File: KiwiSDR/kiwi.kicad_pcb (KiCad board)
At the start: 6 copper layers, 117 x 55 mm, 173 parts, among them J1 TB_2, J2 SMA, J3 SMA, J4 DNL U.FL, J5 DNL U.FL, J6 POWER JACK 2.1MM, T301 CMC 500uH 1A, U1 Artix-7 A35, U101 SE4150L, U104 LP5907 3.3V 250mA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

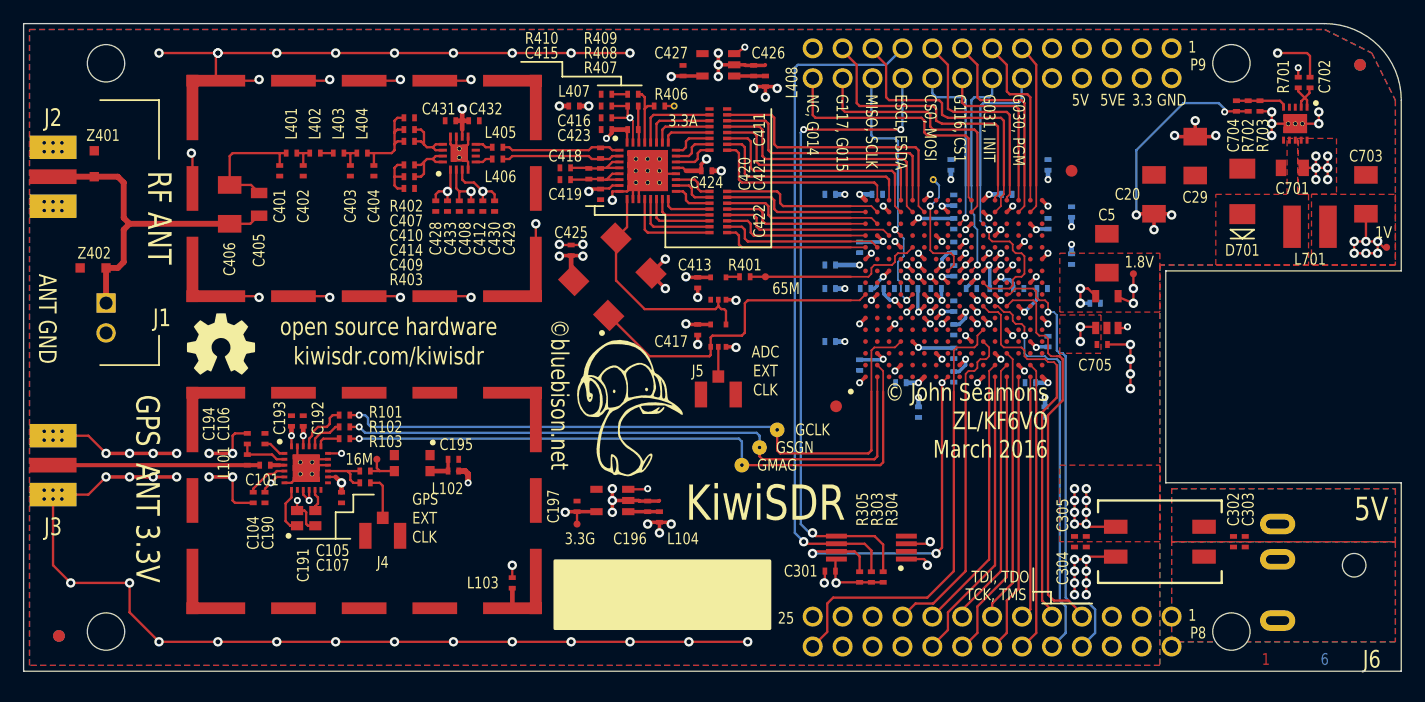
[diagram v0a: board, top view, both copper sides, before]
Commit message: long overdue update to v1.0 PCB files
These are the files used in the current production PCBs.
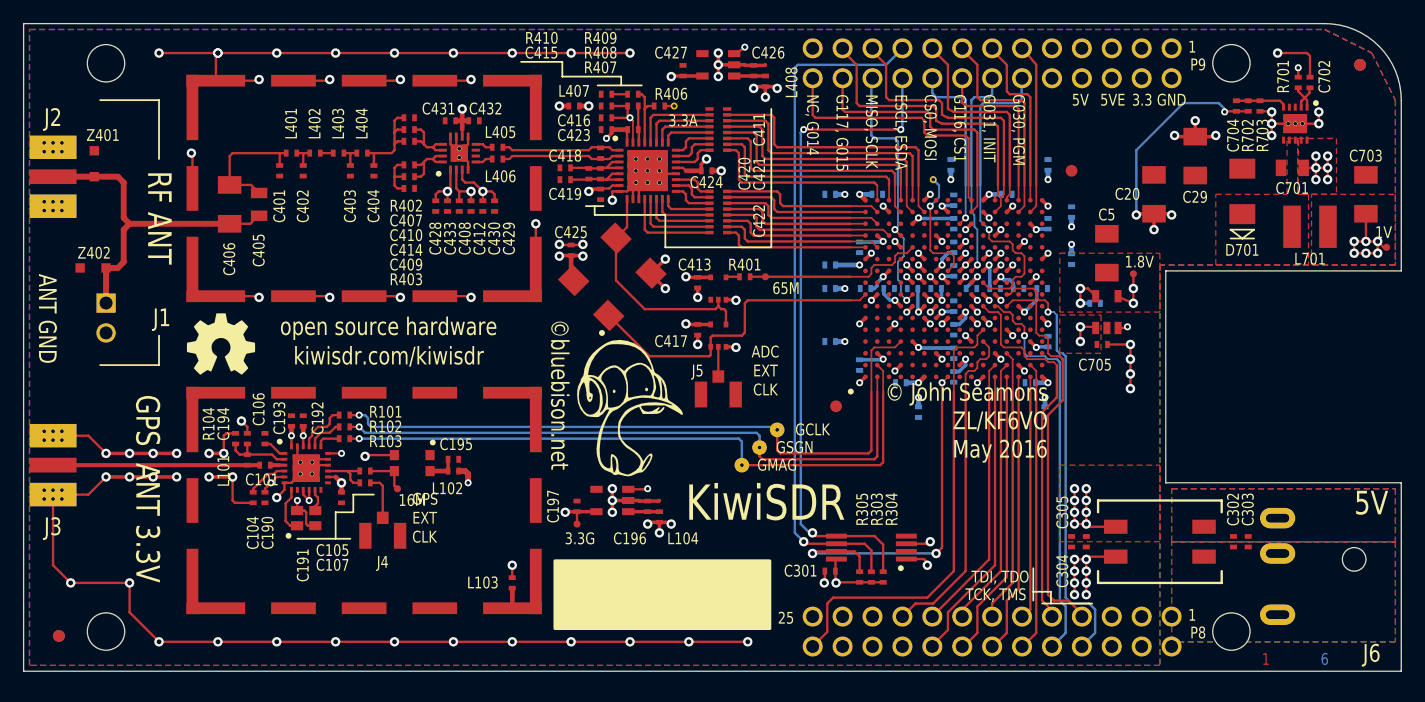
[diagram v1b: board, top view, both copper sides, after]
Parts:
- added R104: 1K5, kiwi-SM0402, F.Cu at (94.0, 107.8)
- moved TP101 3.05 mm to (107.8, 112.0)
- moved J6 0.50 mm to (193.0, 118.0)
- moved C303 0.25 mm to (180.0, 116.5)
- moved C304 0.25 mm to (165.0, 116.5)
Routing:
- net GND: track 296.6 -> 300.9 mm, vias 116 -> 119
- net /GPS/GBIAS: track 4.22 -> 5.91 mm
- net /GPS/TCXO2: track 3.14 -> 3.64 mm
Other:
- board text added: "KiwiSDR V1.0 2-May-2016"
- board text added: "© John Seamons ZL/KF6VO May 2016"
- board text removed: "KiwiSDR prototype v0.5 22-Feb-2016"
- board text removed: "PROTOTYPE ONLY NOT FOR QUANTITY PRODUCTION"
- board text removed: "© John Seamons ZL/KF6VO March 2016"
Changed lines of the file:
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@@
 (kicad_pcb (version 3) (host pcbnew "(2013-mar-25)-stable")
   (general
-    (links 555)
+    (links 557)
     (no_connects 0)
     (area 66.587499 53.8 205.779764 127.775)
     (thickness 1.6)
-    (drawings 73)
-    (tracks 1536)
+    (drawings 72)
+    (tracks 1547)
     (zones 0)
-    (modules 173)
+    (modules 174)
     (nets 120)
   )
@@
   )
   (module kiwi-TP_600 (layer Top)
-    (at 106 109.5)
+    (at 107.75 112)
     (solder_mask_margin 0.05)
     (clearance 0.05)
@@
     (clearance 0.05)
     (attr smd)
-    (fp_text reference C106 (at -1.25 3.5 270) (layer F.SilkS)
+    (fp_text reference C106 (at -2.5 0.5 270) (layer F.SilkS)
       (effects (font (size 1 0.8) (thickness 0.15)))
     )
@@
     (clearance 0.05)
     (attr smd)
-    (fp_text reference L101 (at -0.2 -2 90) (layer F.SilkS)
+    (fp_text reference L101 (at -0.95 -2 90) (layer F.SilkS)
       (effects (font (size 1 0.8) (thickness 0.15)))
     )
@@
     (clearance 0.05)
     (attr smd)
-    (fp_text reference C194 (at -1.25 3.25 270) (layer F.SilkS)
+    (fp_text reference C194 (at -1.25 2 270) (layer F.SilkS)
       (effects (font (size 1 0.8) (thickness 0.15)))
     )
@@
   )
   (module kiwi-SM0402 (layer Top)
-    (at 179.75 116.5 270)
+    (at 180 116.5 270)
     (solder_mask_margin 0.05)
     (clearance 0.05)
     (attr smd)
-    (fp_text reference C303 (at -2.75 -0.25 270) (layer F.SilkS)
+    (fp_text reference C303 (at -2.75 0 270) (layer F.SilkS)
       (effects (font (size 1 0.8) (thickness 0.15)))
     )
@@
   )
   (module kiwi-SM0402 (layer Top)
-    (at 165.25 116.5 270)
+    (at 165 116.5 270)
     (solder_mask_margin 0.05)
     (clearance 0.05)
     (attr smd)
-    (fp_text reference C304 (at 2.25 1 270) (layer F.SilkS)
+    (fp_text reference C304 (at 2.5 0.75 270) (layer F.SilkS)
       (effects (font (size 1 0.8) (thickness 0.15)))
     )
@@
     (clearance 0.05)
     (attr smd)
-    (fp_text reference C305 (at -2.25 2 270) (layer F.SilkS)
+    (fp_text reference C305 (at -2.5 2 270) (layer F.SilkS)
       (effects (font (size 1 0.8) (thickness 0.15)))
     )
@@
   )
   (module kiwi-JACK_2_1MM_TH (layer Top)
-    (at 193 118.5)
+    (at 193 118)
     (descr "Best JACK_2_1MM_TH footprint")
     (solder_mask_margin 0.05)
@@
     )
   )
+  (module kiwi-SM0402 (layer Top)
+    (at 94 107.75 90)
+    (solder_mask_margin 0.05)
+    (clearance 0.05)
+    (attr smd)
+    (fp_text reference R104 (at 1.25 -2.25 90) (layer F.SilkS)
+      (effects (font (size 1 0.8) (thickness 0.15)))
+    )
+    (fp_text value 1K5 (at 0 0 90) (layer F.SilkS) hide
+      (effects (font (size 1 0.8) (thickness 0.15)))
+    )
+    (pad 1 smd rect (at -0.45 0 90) (size 0.4 0.6)
+      (layers Top F.Paste F.Mask)
+      (net 62 /GPS/GBIAS)
+    )
+    (pad 2 smd rect (at 0.45 0 90) (size 0.4 0.6)
+      (layers Top F.Paste F.Mask)
+      (net 116 GND)
+    )
+  )
   (gr_line (start 163.25 120.75) (end 163.25 121.75) (angle 90) (layer F.SilkS) (width 0.15))
   (gr_line (start 161.75 120.75) (end 163.25 120.75) (angle 90) (layer F.SilkS) (width 0.15))
@@
     (effects (font (size 1 0.8) (thickness 0.15)))
   )
-  (gr_text 5V (at 189 113.75) (layer F.SilkS)
+  (gr_text 5V (at 189 113.25) (layer F.SilkS)
     (effects (font (size 2 1.6) (thickness 0.3)) (justify left))
   )
@@
     (effects (font (size 1.5 1.2) (thickness 0.2)))
   )
-  (gr_text "© John Seamons\nZL/KF6VO\nMarch 2016" (at 163 106.25) (layer F.SilkS)
+  (gr_text "© John Seamons\nZL/KF6VO\nMay 2016" (at 163 106.25) (layer F.SilkS)
     (effects (font (size 1.5 1.2) (thickness 0.2)) (justify right))
   )
@@
     (effects (font (size 1.5 1.2) (thickness 0.2)))
   )
-  (gr_text "KiwiSDR prototype v0.5 22-Feb-2016" (at 126 63) (layer Dwgs.User)
-    (effects (font (size 1 0.8) (thickness 0.15)))
-  )
   (gr_text KiwiSDR (at 139 113.25) (layer F.SilkS)
     (effects (font (size 3 2.4) (thickness 0.5)))
@@
     (effects (font (size 1 0.8) (thickness 0.15)))
   )
-  (gr_text "PROTOTYPE ONLY\nNOT FOR QUANTITY PRODUCTION" (at 128 56) (layer Dwgs.User)
+  (gr_text "KiwiSDR\nV1.0 2-May-2016" (at 128 56) (layer Dwgs.User)
     (effects (font (size 2.5 2.5) (thickness 0.3)))
   )
@@
     (effects (font (size 1 0.8) (thickness 0.15)) (justify left))
   )
-  (gr_text 16M (at 104.5 109.5) (layer F.SilkS)
+  (gr_text 16M (at 109 113) (layer F.SilkS)
     (effects (font (size 1 0.8) (thickness 0.15)))
   )
@@
   (segment (start 106.5 111.75) (end 106.5 114.475) (width 0.2) (layer Top) (net 61))
   (segment (start 106.25 111.5) (end 106.5 111.75) (width 0.2) (layer Top) (net 61))
+  (segment (start 95 109.1) (end 94.35 109.1) (width 0.2) (layer Top) (net 62))
+  (segment (start 94 108.75) (end 94 108.2) (width 0.2) (layer Top) (net 62))
+  (segment (start 94.35 109.1) (end 94 108.75) (width 0.2) (layer Top) (net 62))
   (segment (start 95 108.2) (end 95 109.1) (width 0.2) (layer Top) (net 62))
   (segment (start 95 109.1) (end 97.1 109.1) (width 0.2) (layer Top) (net 62))
@@
   (segment (start 103.75 110.75) (end 103.5 110.5) (width 0.2) (layer Top) (net 72))
   (segment (start 101.85 110.5) (end 103.5 110.5) (width 0.2) (layer Top) (net 72))
-  (segment (start 106 109.5) (end 106 110.25) (width 0.2) (layer Top) (net 73))
-  (segment (start 106 110.25) (end 106.25 110.5) (width 0.2) (layer Top) (net 73))
-  (segment (start 105.45 110.5) (end 106.25 110.5) (width 0.2) (layer Top) (net 73))
-  (segment (start 106.25 110.5) (end 107.48 110.5) (width 0.2) (layer Top) (net 73))
-  (segment (start 107.48 110.5) (end 107.485 110.505) (width 0.2) (layer Top) (net 73))
+  (segment (start 107.485 110.505) (end 107.485 111.735) (width 0.2) (layer Top) (net 73))
+  (segment (start 107.485 111.735) (end 107.75 112) (width 0.2) (layer Top) (net 73))
+  (segment (start 107.485 110.505) (end 105.455 110.505) (width 0.2) (layer Top) (net 73))
+  (segment (start 105.455 110.505) (end 105.45 110.5) (width 0.2) (layer Top) (net 73))
   (segment (start 112.05 110.5) (end 112.05 109.5) (width 0.3) (layer Top) (net 74))
   (segment (start 112.05 110.5) (end 110.52 110.5) (width 0.4) (layer Top) (net 74))
@@
   (segment (start 149 102) (end 148.5 101.5) (width 0.15) (layer Top) (net 115))
   (segment (start 149 102) (end 149 103.75) (width 0.15) (layer Top) (net 115))
+  (segment (start 107.485 109.145) (end 105.105 109.145) (width 0.2) (layer Top) (net 116))
+  (via (at 105 109.25) (size 0.8) (drill 0.4) (layers Top Bottom) (net 116))
+  (segment (start 105.105 109.145) (end 105 109.25) (width 0.2) (layer Top) (net 116))
+  (segment (start 98.15 111.5) (end 98.15 112.1) (width 0.2) (layer Top) (net 116))
+  (via (at 97.5 112.75) (size 0.8) (drill 0.4) (layers Top Bottom) (net 116))
+  (segment (start 98.15 112.1) (end 97.5 112.75) (width 0.2) (layer Top) (net 116))
+  (segment (start 95 107.3) (end 95 106.75) (width 0.2) (layer Top) (net 116))
+  (segment (start 95 106.75) (end 94.5 106.25) (width 0.2) (layer Top) (net 116))
+  (via (at 94.5 106.25) (size 0.8) (drill 0.4) (layers Top Bottom) (net 116))
+  (segment (start 94 107.3) (end 93.2 107.3) (width 0.2) (layer Top) (net 116))
+  (segment (start 93 109) (end 91.75 109) (width 0.3) (layer Top) (net 116))
+  (via (at 91.75 109) (size 0.8) (drill 0.4) (layers Top Bottom) (net 116))
+  (via (at 93 109) (size 0.8) (drill 0.4) (layers Top Bottom) (net 116))
+  (segment (start 93 107.5) (end 93 109) (width 0.2) (layer Top) (net 116))
+  (segment (start 93.2 107.3) (end 93 107.5) (width 0.2) (layer Top) (net 116))
   (segment (start 166.25 121) (end 166.25 120) (width 0.2) (layer Top) (net 116))
   (via (at 166.25 120) (size 0.8) (drill 0.4) (layers Top Bottom) (net 116))
@@
   (segment (start 93.75 113) (end 93.75 111) (width 0.2) (layer Top) (net 116))
   (segment (start 93.95 113.2) (end 93.75 113) (width 0.2) (layer Top) (net 116))
-  (segment (start 91.75 109) (end 93.75 109) (width 0.3) (layer Top) (net 116))
-  (via (at 91.75 109) (size 0.8) (drill 0.4) (layers Top Bottom) (net 116))
-  (segment (start 93.95 107.3) (end 95 107.3) (width 0.2) (layer Top) (net 116))
-  (via (at 93.75 109) (size 0.8) (drill 0.4) (layers Top Bottom) (net 116))
-  (segment (start 93.75 107.5) (end 93.75 109) (width 0.2) (layer Top) (net 116))
-  (segment (start 93.95 107.3) (end 93.75 107.5) (width 0.2) (layer Top) (net 116))
   (segment (start 100.775 115.145) (end 100.145 115.145) (width 0.2) (layer Top) (net 116))
   (segment (start 99.855 113.855) (end 100 114) (width 0.2) (layer Top) (net 116))
